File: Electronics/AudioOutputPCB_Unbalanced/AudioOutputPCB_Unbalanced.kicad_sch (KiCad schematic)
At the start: 93 parts, among them J1 IDC Header, J2 RCA x2, J3 RCA x2, J4 RCA x2, J5 RCA x2, U1 NE5532, U2 NE5532, U3 NE5532, U4 NE5532

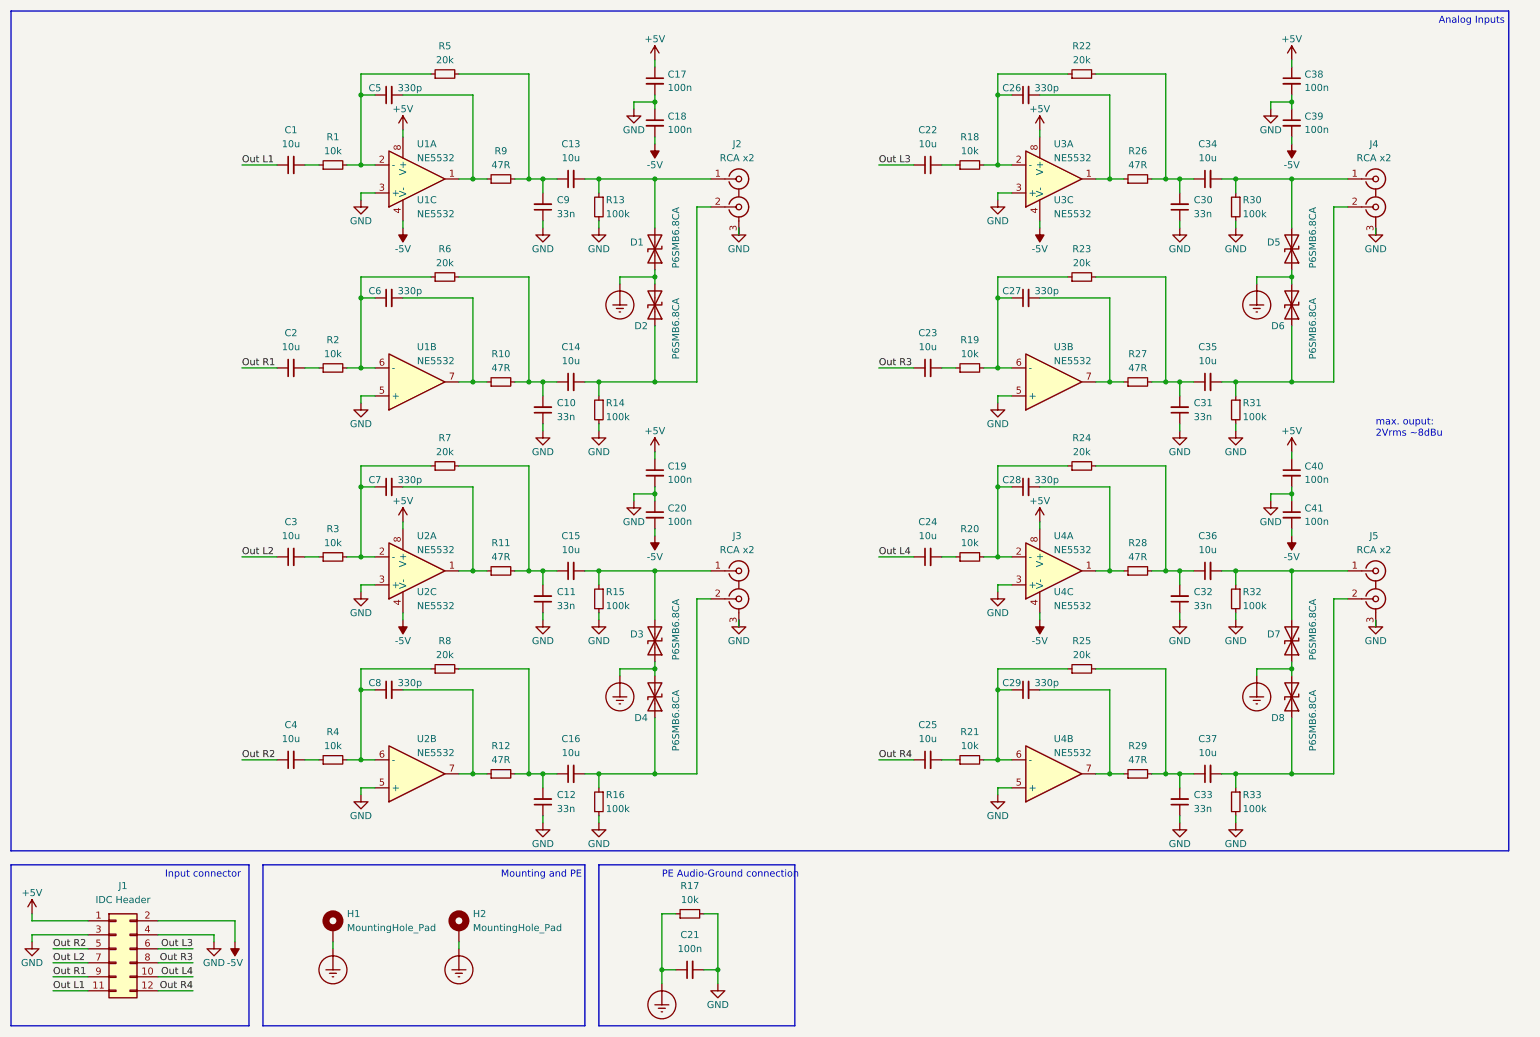
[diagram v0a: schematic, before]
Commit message: Finishes SmallDSP Maxi plus the fitting In- and Output Boards
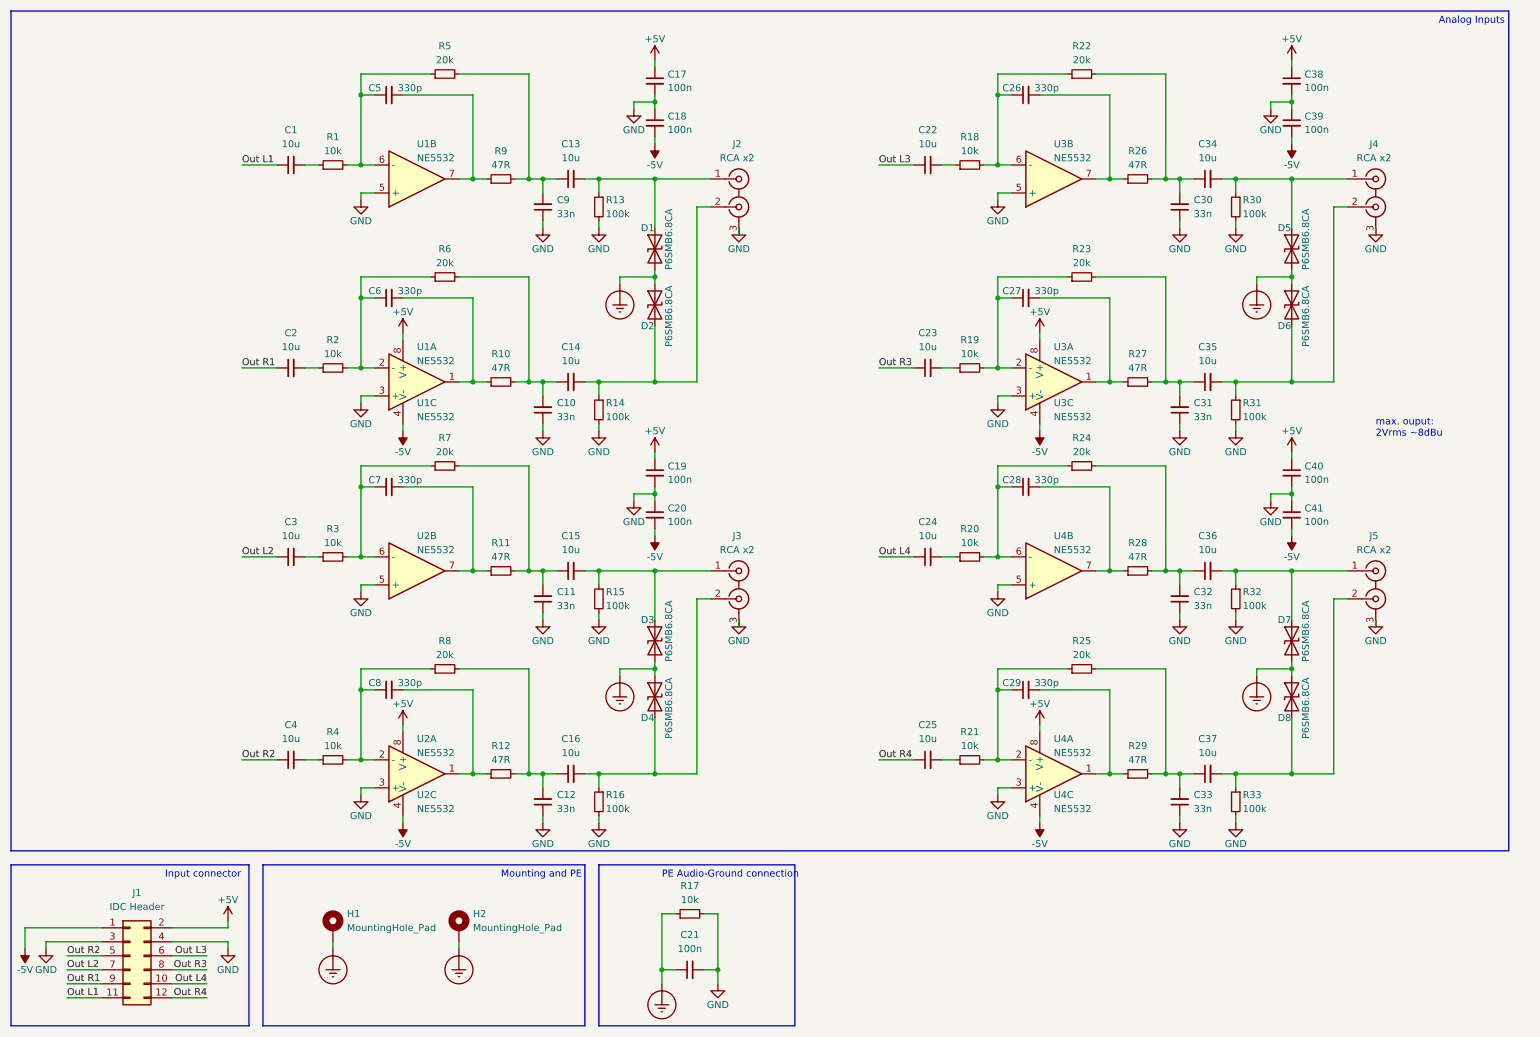
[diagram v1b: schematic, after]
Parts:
- J1: JLC Part Number - -> (none)
- renumbered C9 to C10, C12 to C11, C11 to C12, C14 to C13, C13 to C14, C16 to C15, C15 to C16, C27 to C26, C26 to C27, C29 to C28, C28 to C29, C31 to C30, C30 to C31, C33 to C32, C32 to C33, C35 to C34, C34 to C35, C37 to C36, C36 to C37, C6 to C5, C5 to C6, C8 to C7, C7 to C8, C10 to C9, D2 to D1, D1 to D2, D4 to D3, D3 to D4, D6 to D5, D5 to D6, D8 to D7, D7 to D8, R2 to R1, R9 to R10, R12 to R11, R11 to R12, R14 to R13, R13 to R14, R16 to R15, R15 to R16, R19 to R18, R18 to R19, R1 to R2, R21 to R20, R20 to R21, R23 to R22, R22 to R23, R25 to R24, R24 to R25, R27 to R26, R26 to R27, R29 to R28, R28 to R29, R4 to R3, R31 to R30, R30 to R31, R33 to R32, R32 to R33, R3 to R4, R6 to R5, R5 to R6, R8 to R7, R7 to R8, R10 to R9
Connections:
- net +5V: now also J1.2 (Pin_2); no longer J1.1 (Pin_1)
- net -5V: now also J1.1 (Pin_1); no longer J1.2 (Pin_2)
- net at C16.2, D4.2 (A2), R16.1: now also J3.2 (IN2); no longer J3.1 (IN1)
- net at R20.1: now also C24.2; no longer C25.2
- net at C13.2, D1.1 (A1), R13.1: now also J2.1 (IN1); no longer J2.2 (IN2)
- net at C14.2, D2.2 (A2), R14.1: now also J2.2 (IN2); no longer J2.1 (IN1)
- net at C37.2, D8.2 (A2), R33.1: now also J5.2 (IN2); no longer J5.1 (IN1)
- net at C36.2, D7.1 (A1), R32.1: now also J5.1 (IN1); no longer J5.2 (IN2)
- net at C15.2, D3.1 (A1), R15.1: now also J3.1 (IN1); no longer J3.2 (IN2)
- net at R3.1: now also C3.2; no longer C4.2
- net at C35.2, D6.2 (A2), R31.1: now also J4.2 (IN2); no longer J4.1 (IN1)
- net at R4.1: now also C4.2; no longer C3.2
- net at R2.1: now also C2.2; no longer C1.2
- net at C23.2: now also R19.1; no longer R18.1
- net at C22.2: now also R18.1; no longer R19.1
- net at R21.1: now also C25.2; no longer C24.2
- net at C34.2, D5.1 (A1), R30.1: now also J4.1 (IN1); no longer J4.2 (IN2)
- net at R1.1: now also C1.2; no longer C2.2
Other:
- moved on the sheet: C10, C11, C12, C13, C14, C15, C16, C26, C27, C28, C29, C30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

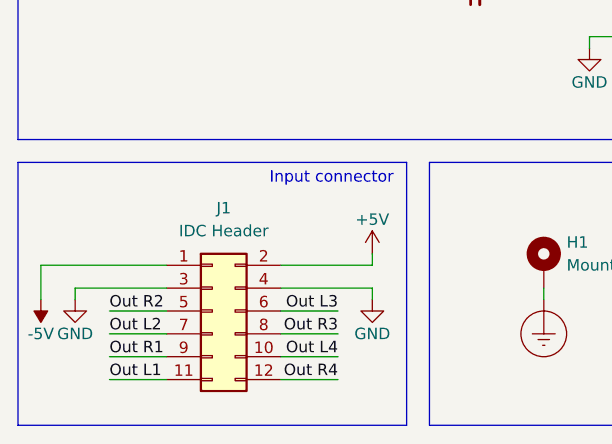
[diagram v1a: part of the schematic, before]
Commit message: replaces 12pin IDC out header with 14pin one because of better availability.
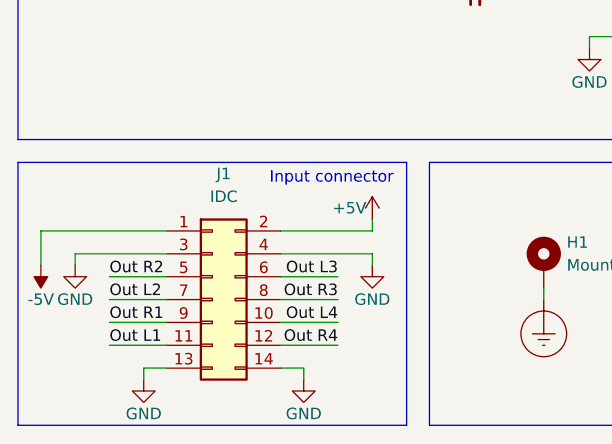
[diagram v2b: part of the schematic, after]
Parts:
- removed J1: IDC Header, Connector_IDC:IDC-Header_2x06_P2.54mm_Vertical, symbol Connector_Generic:Conn_02x06_Odd_Even
- added J1: IDC, Connector_IDC:IDC-Header_2x07_P2.54mm_Vertical, symbol Connector_Generic:Conn_02x07_Odd_Even
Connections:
- net +5V: now also J1.2 (Pin_2)
- net -5V: now also J1.1 (Pin_1)
- net GND: now also J1.13 (Pin_13), J1.14 (Pin_14), J1.3 (Pin_3), J1.4 (Pin_4)
- net Out L1: now also J1.11 (Pin_11)
- net Out L2: now also J1.7 (Pin_7)
- net Out L3: now also J1.6 (Pin_6)
- net Out L4: now also J1.10 (Pin_10)
- net Out R1: now also J1.9 (Pin_9)
- net Out R2: now also J1.5 (Pin_5)
- net Out R3: now also J1.8 (Pin_8)
- net Out R4: now also J1.12 (Pin_12)

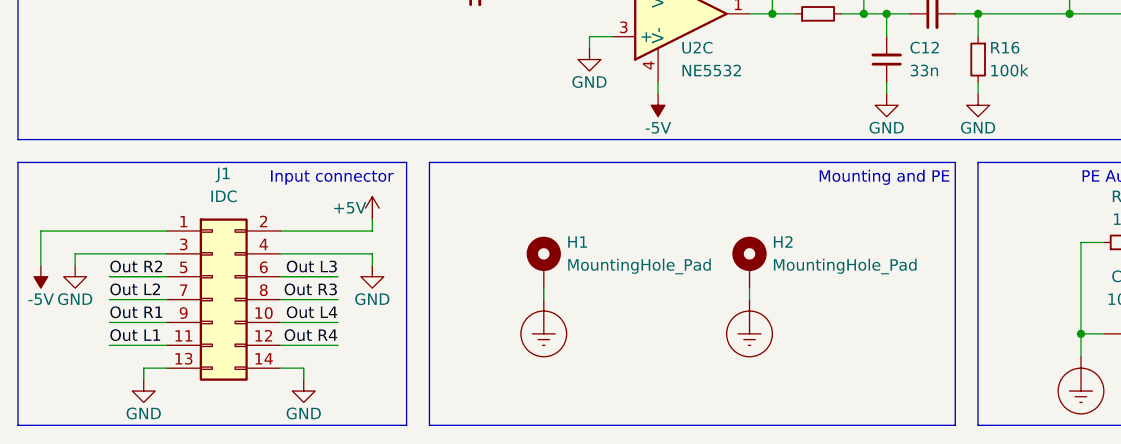
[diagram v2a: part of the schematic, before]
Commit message: adds usb to i2s bridge to micro. Adds tweaks for layout of maxi.
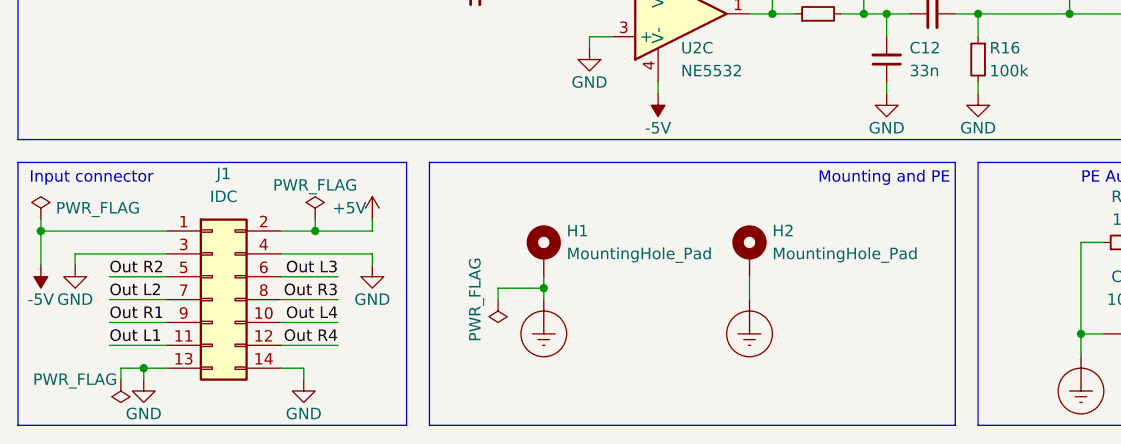
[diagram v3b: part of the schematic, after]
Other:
- moved on the sheet: H1, H2

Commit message: Adds final state of Maxi rev 1.0 and unbalanced IO boards rev 1.0.
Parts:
- D1, D2, D3, D4, D5, D6, D7, D8: value P6SMB6.8CA -> H5VL10B; footprint Diode_SMD:D_SMB -> 1_Project_Footprints:DFN1006-2; JLC Part Number C78395 -> (none); LCSC Part # C78395 -> C7420372; Manufacturer Brightking -> hongjiacheng; Part Number P6SMB6.8CA/TR13 -> H5VL10B

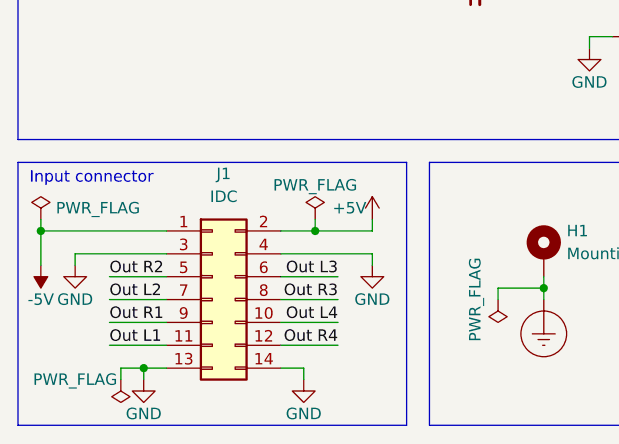
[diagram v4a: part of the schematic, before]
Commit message: Maxi: Replaces STM32 programming pin header with WE RedFit connectorand fixes minor issues. Adds driver for AKM AK4619 Codec and STM32CubeIDE workspace for Maxi firmware.
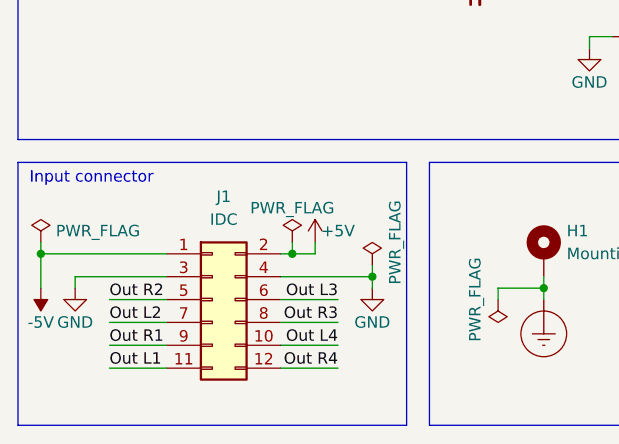
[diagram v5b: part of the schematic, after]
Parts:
- removed J1: IDC, Connector_IDC:IDC-Header_2x07_P2.54mm_Vertical, symbol Connector_Generic:Conn_02x07_Odd_Even
- added J1: IDC, Connector_IDC:IDC-Header_2x06_P2.54mm_Vertical, symbol Connector_Generic:Conn_02x06_Odd_Even
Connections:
- net +5V: now also J1.2 (Pin_2)
- net -5V: now also J1.1 (Pin_1)
- net GND: now also J1.3 (Pin_3), J1.4 (Pin_4)
- net Out L1: now also J1.11 (Pin_11)
- net Out L2: now also J1.7 (Pin_7)
- net Out L3: now also J1.6 (Pin_6)
- net Out L4: now also J1.10 (Pin_10)
- net Out R1: now also J1.9 (Pin_9)
- net Out R2: now also J1.5 (Pin_5)
- net Out R3: now also J1.8 (Pin_8)
- net Out R4: now also J1.12 (Pin_12)

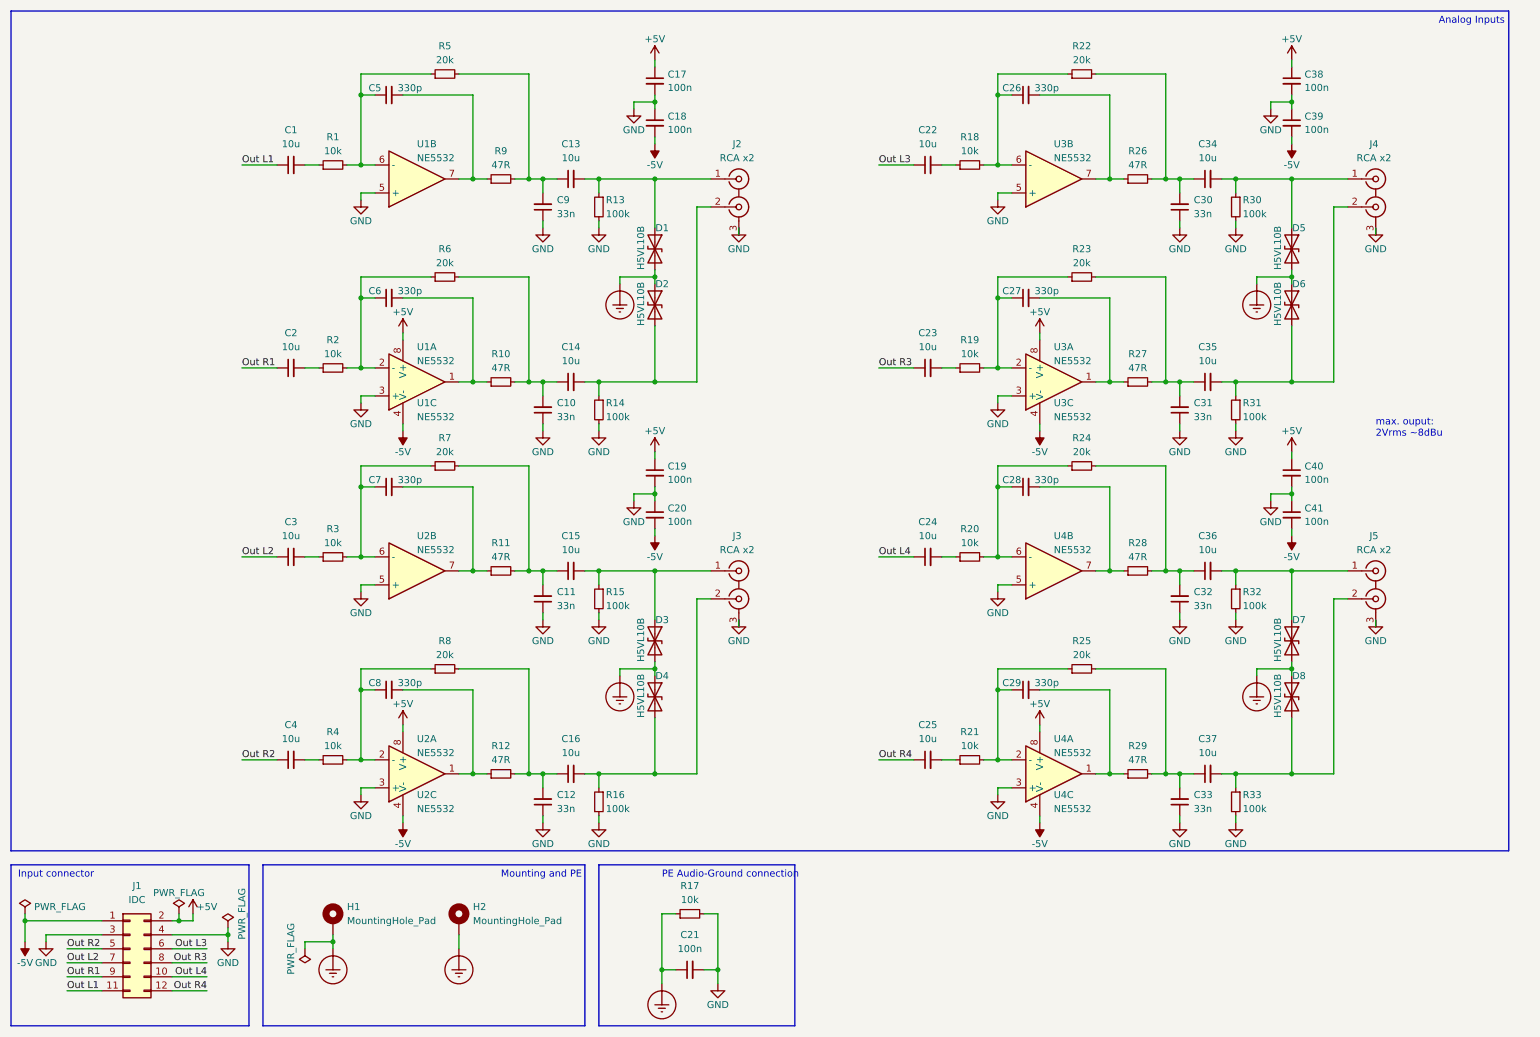
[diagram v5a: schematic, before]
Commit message: Adds AES17 measurements for rev1 of maxi. adds first iteration of maxi firmware. prototype now functional. adds mechanical information such as pcb 3d models and datasheets for psu and power switch, -connector.
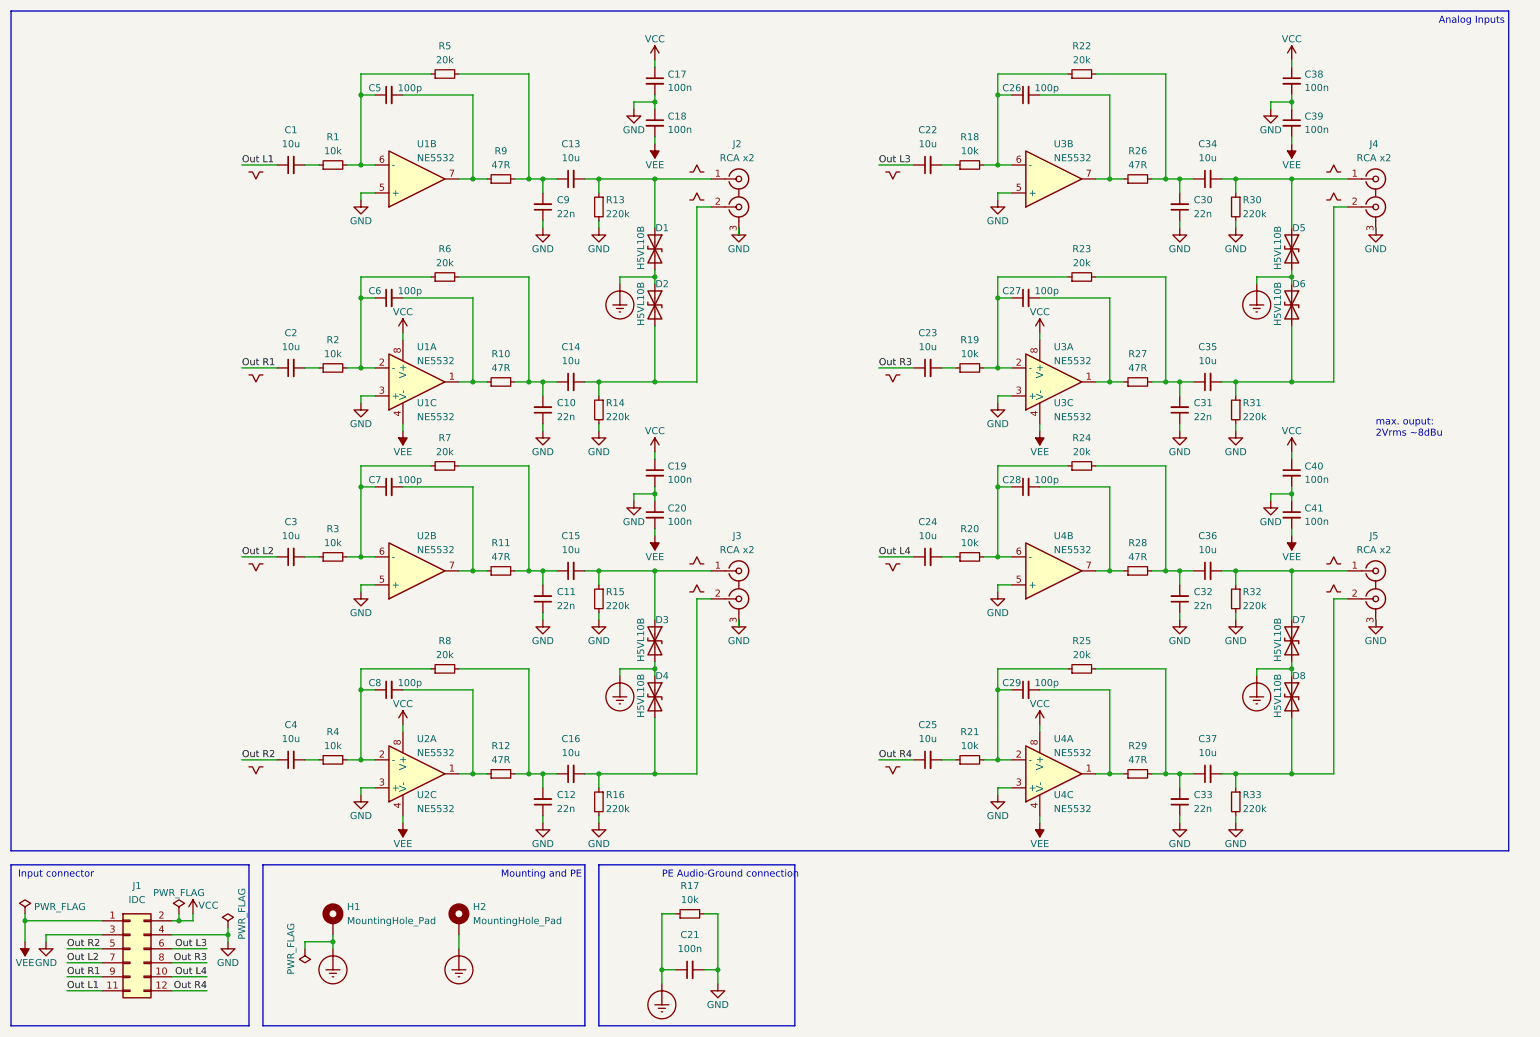
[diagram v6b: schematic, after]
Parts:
- added Label1, Label10, Label11, Label12, Label13, Label14, Label15, Label16, Label2, Label3, Label4, Label5, Label6, Label7, Label8, Label9: ~, symbol 1_Project_Symbols:phase
- C1, C13, C14, C15, C16, C2, C22, C23, C24, C25, C3, C34, C35, C36, C37, C4: LCSC Part # C13585 -> (none)
- C10, C11, C12, C30, C31, C32, C33, C9: value 33n -> 22n; JLC Part Number C21117 -> C21122; LCSC Part # C21117 -> (none); Part Number CL10B333KB8NNNC -> CL10B223KB8NNNC
- C17, C18, C19, C20, C21, C38, C39, C40, C41: LCSC Part # C307331 -> (none)
- C26, C27, C28, C29, C5, C6, C7, C8: value 330p -> 100p; JLC Part Number C13533 -> C1546; LCSC Part # C13533 -> (none); Manufacturer Samsung Electro-Mechanics -> FH (Guangdong Fenghua Advanced Tech); Part Number CL05C331JB5NNNC -> 0402CG101J500NT
- D1, D2, D3, D4, D5, D6, D7, D8: LCSC Part # C7420372 -> (none)
- H1, H2, J1, J2, J3, J4, J5: LCSC Part # - -> (none)
- R1, R17, R18, R19, R2, R20, R21, R3, R4: LCSC Part # C25744 -> (none)
- R10, R11, R12, R26, R27, R28, R29, R9: LCSC Part # C25118 -> (none)
- R13, R14, R15, R16, R30, R31, R32, R33: value 100k -> 220k; JLC Part Number C25741 -> C25767; LCSC Part # C25741 -> (none); Part Number 0402WGF1003TCE -> 0402WGF2203TCE
- R22, R23, R24, R25, R5, R6, R7, R8: LCSC Part # C25765 -> (none)
- U1, U2, U3, U4: LCSC Part # C7426 -> (none)
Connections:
- net +5V renamed VCC
- net -5V renamed VEE
